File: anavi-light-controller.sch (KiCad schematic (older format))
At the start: 18 parts, among them J1 Screw_Terminal_1x04, P1 CONN_01X03, Q1 IRF8721PBF-1, Q2 IRF8721PBF-1, Q3 IRF8721PBF-1, SW1 SW_DIP_x01, U1 I2C_SENS_1, U2 I2C_SENS_1, U3 I2C_SENS_1

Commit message: Change LDO voltage regulator
Use LD1117S33TR as LDO voltage regulator to drop
from 12V to 3.3V and to power the ESP8266 module.

Signed-off-by: Leon Anavi <leon@anavi.org>
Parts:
- removed L1: 78L33, smd-semi:SOT-89, symbol 78L33
- added R4, R5, R6: 220R, Resistors_SMD:R_0603_HandSoldering, symbol R
- added V1: LD1117S33TR, SOT-223, symbol LD1117S33TR
- C1: value C -> 100nF
- C2: value C -> 10uF; footprint Capacitors_SMD:C_0603_HandSoldering -> Capacitors_SMD:C_0805_HandSoldering
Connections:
- net +12V: now also V1.3 (VI)
- net +3V3: now also V1.2 (VO)
- net GND: now also V1.1 (GND)
- net at ESP-12.5 (GPIO14): now also R4.2; no longer Q3.4 (G)
- net at ESP-12.6 (GPIO12): now also R5.2; no longer Q2.4 (G)
- net at ESP-12.7 (GPIO13): now also R6.2; no longer Q1.4 (G)
- new net: Q3.4 (G), R4.1
- new net: Q2.4 (G), R5.1
- new net: Q1.4 (G), R6.1
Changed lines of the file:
@@
 NoConn ~ 2950 5100
-$Comp
-L 78L33 L1
-U 1 1 598B19AF
-P 1800 2050
-F 0 "L1" H 1950 1854 50  0000 C CNN
-F 1 "78L33" H 1800 2250 50  0000 C CNN
-F 2 "smd-semi:SOT-89" H 1800 2050 50  0001 C CNN
-F 3 "" H 1800 2050 50  0000 C CNN
-	1    1800 2050
-	1    0    0    -1
-$EndComp
 $Comp
 L C C1
@@
 P 1200 2200
 F 0 "C1" H 1225 2300 50  0000 L CNN
-F 1 "C" H 1225 2100 50  0000 L CNN
+F 1 "100nF" H 1225 2100 50  0000 L CNN
 F 2 "Capacitors_SMD:C_0603_HandSoldering" H 1238 2050 50  0001 C CNN
 F 3 "" H 1200 2200 50  0000 C CNN
@@
 P 2350 2200
 F 0 "C2" H 2375 2300 50  0000 L CNN
-F 1 "C" H 2375 2100 50  0000 L CNN
-F 2 "Capacitors_SMD:C_0603_HandSoldering" H 2388 2050 50  0001 C CNN
+F 1 "10uF" H 2375 2100 50  0000 L CNN
+F 2 "Capacitors_SMD:C_0805_HandSoldering" H 2388 2050 50  0001 C CNN
 F 3 "" H 2350 2200 50  0000 C CNN
 	1    2350 2200
@@
 	2850 3300 2850 2900
 Wire Wire Line
-	2850 2900 4800 2900
-Wire Wire Line
 	4800 2900 4800 3500
 Wire Wire Line
 	2950 3300 2950 2600
 Wire Wire Line
-	2950 2600 4800 2600
-Wire Wire Line
 	3050 3300 3050 1600
-Wire Wire Line
-	3050 1600 4800 1600
 Wire Wire Line
 	1200 2350 2350 2350
@@
 Connection ~ 1800 2350
 Wire Wire Line
-	2200 2000 2550 2000
-Wire Wire Line
 	2350 2050 2350 2000
 Connection ~ 2350 2000
@@
 Wire Wire Line
 	1200 1300 1200 2050
-Wire Wire Line
-	1400 2000 1200 2000
 Connection ~ 1200 2000
 Wire Wire Line
@@
 $EndComp
 Connection ~ 1200 1300
+$Comp
+L R R4
+U 1 1 5991CFCD
+P 4400 1600
+F 0 "R4" V 4480 1600 50  0000 C CNN
+F 1 "220R" V 4400 1600 50  0000 C CNN
+F 2 "Resistors_SMD:R_0603_HandSoldering" V 4330 1600 50  0001 C CNN
+F 3 "" H 4400 1600 50  0000 C CNN
+	1    4400 1600
+	0    1    1    0
+$EndComp
+$Comp
+L R R5
+U 1 1 5991D06A
+P 4400 2600
+F 0 "R5" V 4480 2600 50  0000 C CNN
+F 1 "220R" V 4400 2600 50  0000 C CNN
+F 2 "Resistors_SMD:R_0603_HandSoldering" V 4330 2600 50  0001 C CNN
+F 3 "" H 4400 2600 50  0000 C CNN
+	1    4400 2600
+	0    1    1    0
+$EndComp
+$Comp
+L R R6
+U 1 1 5991D0D3
+P 4400 2900
+F 0 "R6" V 4480 2900 50  0000 C CNN
+F 1 "220R" V 4400 2900 50  0000 C CNN
+F 2 "Resistors_SMD:R_0603_HandSoldering" V 4330 2900 50  0001 C CNN
+F 3 "" H 4400 2900 50  0000 C CNN
+	1    4400 2900
+	0    1    1    0
+$EndComp
+Wire Wire Line
+	4550 1600 4800 1600
+Wire Wire Line
+	3050 1600 4250 1600
+Wire Wire Line
+	4550 2600 4800 2600
+Wire Wire Line
+	2950 2600 4250 2600
+Wire Wire Line
+	4550 2900 4800 2900
+Wire Wire Line
+	2850 2900 4250 2900
+$Comp
+L LD1117S33TR V1
+U 1 1 59B80669
+P 1800 2050
+F 0 "V1" H 1800 2300 50  0000 C CNN
+F 1 "LD1117S33TR" H 1800 2250 50  0000 C CNN
+F 2 "SOT-223" H 1800 2150 50  0000 C CNN
+F 3 "" H 1800 2050 50  0000 C CNN
+	1    1800 2050
+	1    0    0    -1
+$EndComp
+Wire Wire Line
+	2200 2000 2550 2000
+Wire Wire Line
+	1400 2000 1200 2000
 $EndSCHEMATC

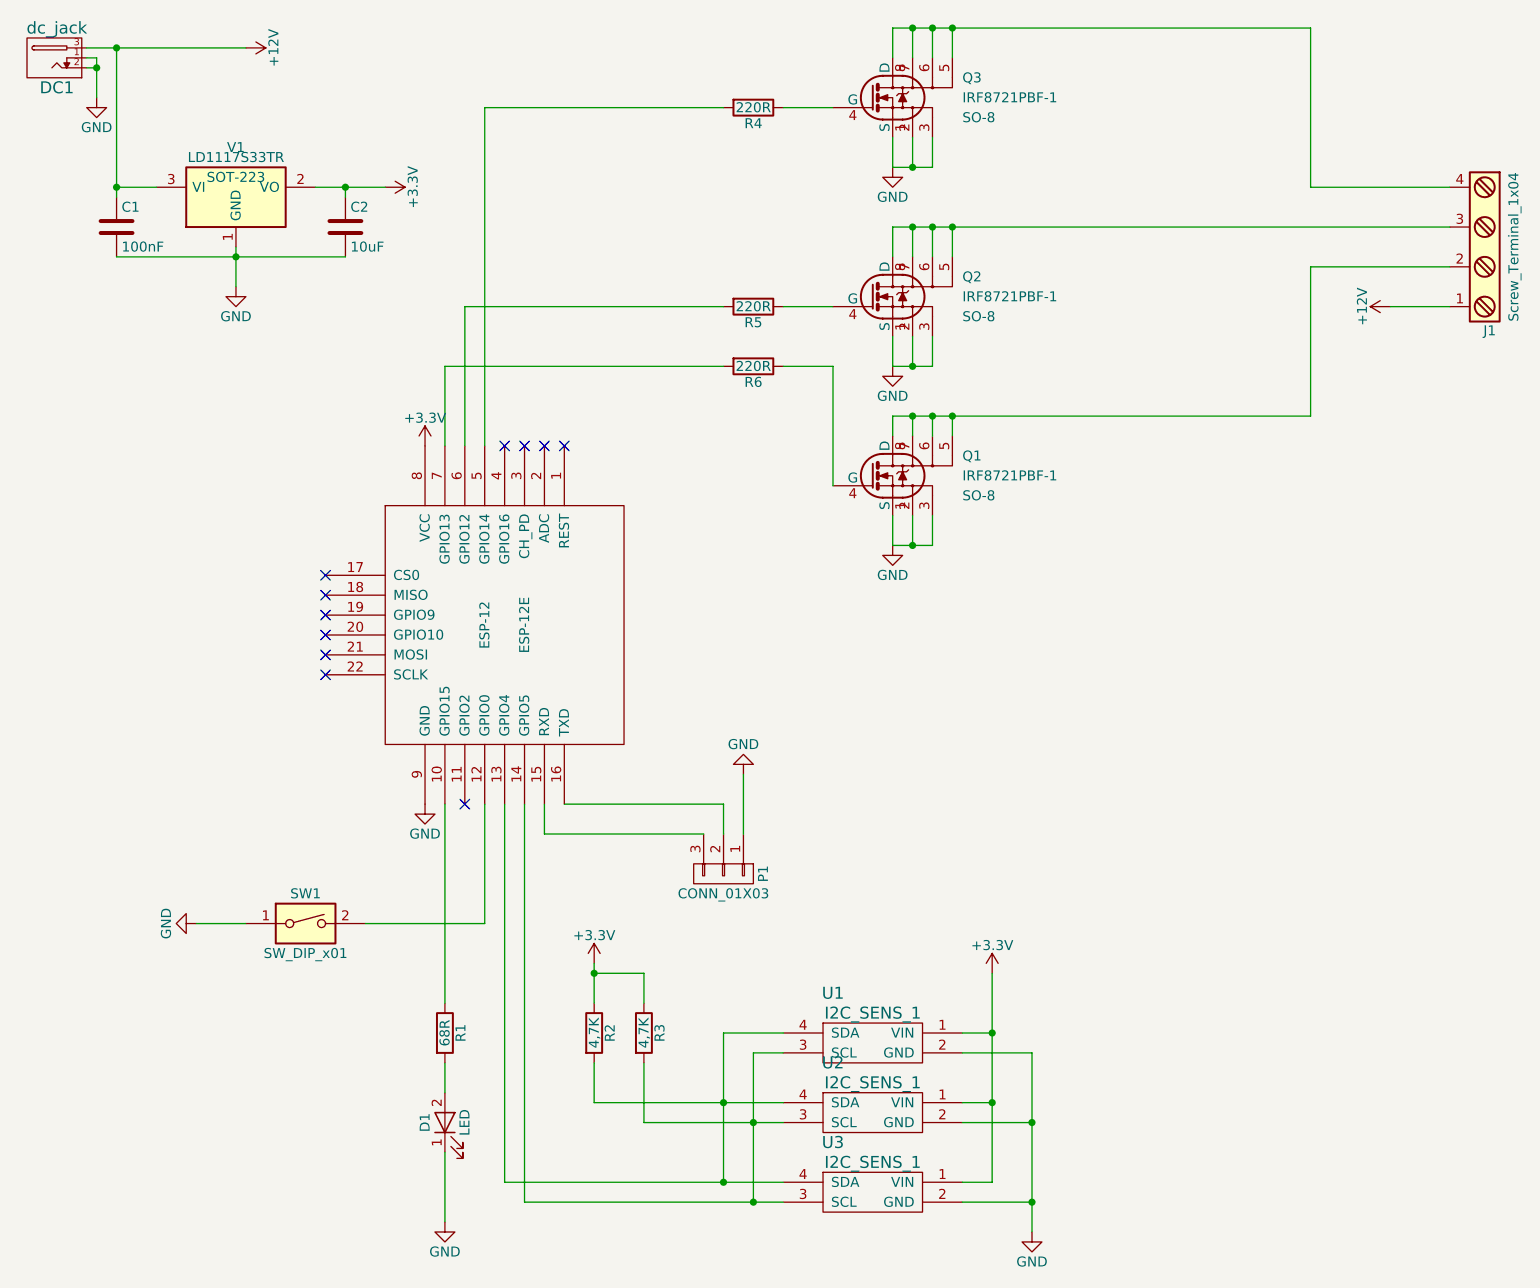
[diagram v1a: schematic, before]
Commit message: Enable ESP-12; Fix the button and LED
Enable ESP-12 by connecting GPIO5 to GND and CH_PD
to 3.3V. Add 2K resistor to GPIO0 to fix the button
and move the alarm LED on the other side.

Signed-off-by: Leon Anavi <leon@anavi.org>
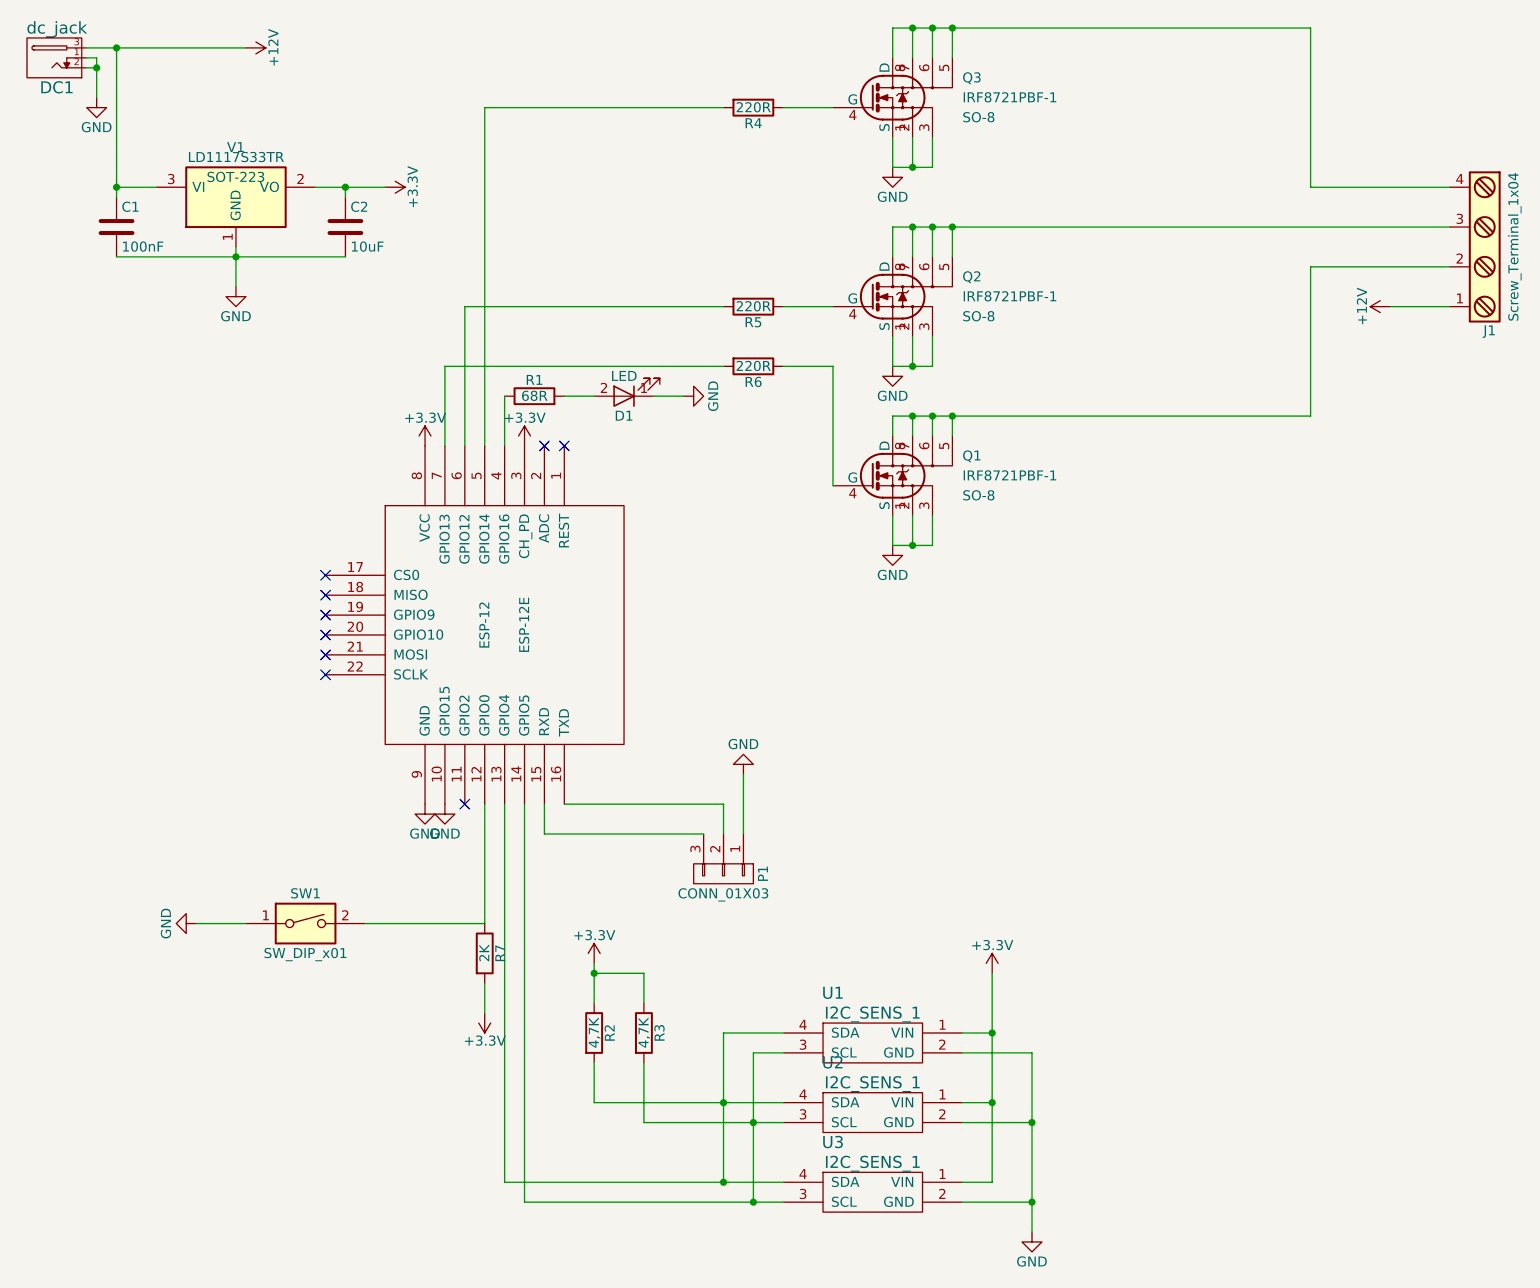
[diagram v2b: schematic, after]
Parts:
- added R7: 2K, Capacitors_SMD:C_0603_HandSoldering, symbol R
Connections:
- net +3V3: now also ESP-12.3 (CH_PD), R7.2
- net GND: now also ESP-12.10 (GPIO15)
- net at R1.1: now also ESP-12.4 (GPIO16); no longer ESP-12.10 (GPIO15)
- net at ESP-12.12 (GPIO0), SW1.2: now also R7.1
- no-connect marks 11 -> 9
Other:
- moved on the sheet: D1, R1
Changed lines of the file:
@@
 L LED D1
 U 1 1 598AC94C
-P 2850 6700
-F 0 "D1" H 2850 6800 50  0000 C CNN
-F 1 "LED" H 2850 6600 50  0000 C CNN
-F 2 "LEDs:LED_1206" H 2850 6700 50  0001 C CNN
-F 3 "" H 2850 6700 50  0000 C CNN
-	1    2850 6700
-	0    -1   -1   0
+P 3750 3050
+F 0 "D1" H 3750 3150 50  0000 C CNN
+F 1 "LED" H 3750 2950 50  0000 C CNN
+F 2 "LEDs:LED_1206" H 3750 3050 50  0001 C CNN
+F 3 "" H 3750 3050 50  0000 C CNN
+	1    3750 3050
+	-1   0    0    1
 $EndComp
 $Comp
@@
 L R R1
 U 1 1 598ADC31
-P 2850 6250
-F 0 "R1" V 2930 6250 50  0000 C CNN
-F 1 "68R" V 2850 6250 50  0000 C CNN
-F 2 "Resistors_SMD:R_0603_HandSoldering" V 2780 6250 50  0001 C CNN
-F 3 "" H 2850 6250 50  0000 C CNN
-	1    2850 6250
-	1    0    0    -1
+P 3300 3050
+F 0 "R1" V 3380 3050 50  0000 C CNN
+F 1 "68R" V 3300 3050 50  0000 C CNN
+F 2 "Resistors_SMD:R_0603_HandSoldering" V 3230 3050 50  0001 C CNN
+F 3 "" H 3300 3050 50  0000 C CNN
+	1    3300 3050
+	0    -1   -1   0
 $EndComp
 $Comp
@@
 L GND #PWR05
 U 1 1 598AFCFA
-P 2850 7200
-F 0 "#PWR05" H 2850 6950 50  0001 C CNN
-F 1 "GND" H 2850 7050 50  0000 C CNN
-F 2 "" H 2850 7200 50  0000 C CNN
-F 3 "" H 2850 7200 50  0000 C CNN
-	1    2850 7200
-	1    0    0    -1
+P 4050 3050
+F 0 "#PWR05" H 4050 2800 50  0001 C CNN
+F 1 "GND" H 4050 2900 50  0000 C CNN
+F 2 "" H 4050 3050 50  0000 C CNN
+F 3 "" H 4050 3050 50  0000 C CNN
+	1    4050 3050
+	0    -1   -1   0
 $EndComp
 $Comp
@@
 	1    0    0    -1
 $EndComp
-NoConn ~ 3150 3300
-NoConn ~ 3250 3300
 NoConn ~ 3350 3300
 NoConn ~ 3450 3300
@@
 Connection ~ 3600 5950
 Wire Wire Line
-	2850 6400 2850 6550
-Wire Wire Line
-	2850 6850 2850 7200
-Wire Wire Line
-	2850 5100 2850 6100
+	3450 3050 3600 3050
 Wire Wire Line
 	3350 5100 3350 5250
@@
 Connection ~ 5400 3150
 Wire Wire Line
-	7900 2200 5100 2200
+	5100 2200 7900 2200
 Wire Wire Line
 	5100 2200 5100 2350
@@
 Wire Wire Line
 	1600 5700 1850 5700
-Wire Wire Line
-	2450 5700 3050 5700
-Wire Wire Line
-	3050 5700 3050 5100
 $Comp
 L +12V #PWR016
@@
 Wire Wire Line
 	1400 2000 1200 2000
+Wire Wire Line
+	3150 3300 3150 3050
+Wire Wire Line
+	3900 3050 4050 3050
+$Comp
+L +3.3V #PWR?
+U 1 1 59B80E88
+P 3250 3300
+F 0 "#PWR?" H 3250 3150 50  0001 C CNN
+F 1 "+3.3V" H 3250 3440 50  0000 C CNN
+F 2 "" H 3250 3300 50  0000 C CNN
+F 3 "" H 3250 3300 50  0000 C CNN
+	1    3250 3300
+	1    0    0    -1
+$EndComp
+$Comp
+L GND #PWR?
+U 1 1 59B811E0
+P 2850 5100
+F 0 "#PWR?" H 2850 4850 50  0001 C CNN
+F 1 "GND" H 2850 4950 50  0000 C CNN
+F 2 "" H 2850 5100 50  0000 C CNN
+F 3 "" H 2850 5100 50  0000 C CNN
+	1    2850 5100
+	1    0    0    -1
+$EndComp
+$Comp
+L R R7
+U 1 1 59B813FF
+P 3050 5850
+F 0 "R7" V 3130 5850 50  0000 C CNN
+F 1 "2K" V 3050 5850 50  0000 C CNN
+F 2 "Capacitors_SMD:C_0603_HandSoldering" V 2980 5850 50  0001 C CNN
+F 3 "" H 3050 5850 50  0000 C CNN
+	1    3050 5850
+	1    0    0    -1
+$EndComp
+$Comp
+L +3.3V #PWR?
+U 1 1 59B81737
+P 3050 6150
+F 0 "#PWR?" H 3050 6000 50  0001 C CNN
+F 1 "+3.3V" H 3050 6290 50  0000 C CNN
+F 2 "" H 3050 6150 50  0000 C CNN
+F 3 "" H 3050 6150 50  0000 C CNN
+	1    3050 6150
+	-1   0    0    1
+$EndComp
+Wire Wire Line
+	3050 5700 3050 5100
+Wire Wire Line
+	2450 5700 3050 5700
+Wire Wire Line
+	3050 6000 3050 6150
 $EndSCHEMATC

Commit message: rev1.2: Use SMD footprint for ESP-12E
Use SMD footprint for ESP-12E to simplify the
assembly, updated product version and routing.

Signed-off-by: Leon Anavi <leon@anavi.org>
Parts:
- ESP-12: footprint ESP8266:ESP-12E -> ESP8266:ESP-12E_SMD
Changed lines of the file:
@@
 F 0 "ESP-12" H 3150 4100 50  0000 C CNN
 F 1 "ESP-12E" H 3150 4300 50  0000 C CNN
-F 2 "ESP8266:ESP-12E" H 3150 4200 50  0001 C CNN
+F 2 "ESP8266:ESP-12E_SMD" H 3150 4200 50  0001 C CNN
 F 3 "" H 3150 4200 50  0001 C CNN
 	1    3150 4200
@@
 	3900 3050 4050 3050
 $Comp
-L +3.3V #PWR?
+L +3.3V #PWR017
 U 1 1 59B80E88
 P 3250 3300
-F 0 "#PWR?" H 3250 3150 50  0001 C CNN
+F 0 "#PWR017" H 3250 3150 50  0001 C CNN
 F 1 "+3.3V" H 3250 3440 50  0000 C CNN
 F 2 "" H 3250 3300 50  0000 C CNN
@@
 $EndComp
 $Comp
-L GND #PWR?
+L GND #PWR018
 U 1 1 59B811E0
 P 2850 5100
-F 0 "#PWR?" H 2850 4850 50  0001 C CNN
+F 0 "#PWR018" H 2850 4850 50  0001 C CNN
 F 1 "GND" H 2850 4950 50  0000 C CNN
 F 2 "" H 2850 5100 50  0000 C CNN
@@
 $EndComp
 $Comp
-L +3.3V #PWR?
+L +3.3V #PWR019
 U 1 1 59B81737
 P 3050 6150
-F 0 "#PWR?" H 3050 6000 50  0001 C CNN
+F 0 "#PWR019" H 3050 6000 50  0001 C CNN
 F 1 "+3.3V" H 3050 6290 50  0000 C CNN
 F 2 "" H 3050 6150 50  0000 C CNN
